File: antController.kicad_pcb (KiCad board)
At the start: 2 copper layers, 230 x 160 mm, 368 parts, among them J1 Lichtenprog_conn, J10 DB25_Male_MountingHoles, J11 DB25_Male_MountingHoles, J12 DB25_Male_MountingHoles, J13 DB25_Male_MountingHoles, J14 goldpins, J2 IDC10, J3 PWRINS, J4 DISP_OLED, J5 SMA CONN, J6 IDC10, J7 Lichtenprog_conn, J8 IDC10, J9 IDC10, K1 G5V-1, K10 G5V-1, K11 G5V-1, K12 G5V-1, K13 G5V-1, K14 G5V-1, K15 G5V-1, K2 G5V-1, K3 G5V-1, K4 G5V-1, K5 G5V-1, K6 G5V-1, K7 G5V-1, K8 G5V-1, K9 G5V-1, Q1 MMBT2222A, Q1 MMBT3904, Q10 BUZ11, Q11 BUZ11, Q12 BUZ11, Q13 BUZ11, Q14 BUZ11, Q15 BUZ11, Q16 BUZ11, Q17 BUZ11, Q18 BUZ11, Q19 2N7002, Q19 MMBT2222A, Q2 MMBT2222A, Q2 MMBT3904, Q20 2N7002, Q20 MMBT2222A, Q21 2N7002, Q21 MMBT2222A, Q22 2N7002, Q22 MMBT2222A, Q23 2N7002, Q23 MMBT2222A, Q24 2N7002, Q24 MMBT2222A, Q25 2N7002, Q25 MMBT2222A, Q26 2N7002, Q26 MMBT2222A, Q27 2N7002, Q27 MMBT2222A, Q28 2N7002, Q28 MMBT2222A, Q29 2N7002, Q29 MMBT2222A, Q3 BUZ11, Q30 2N7002, Q30 MMBT2222A, Q31 2N7002, Q31 MMBT2222A, Q32 2N7002, Q32 MMBT2222A, Q33 2N7002, Q33 MMBT2222A, Q4 BUZ11, Q5 BUZ11, Q6 BUZ11, Q7 BUZ11, Q8 BUZ11, Q9 BUZ11, SW1 B_RST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

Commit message: routing mostly done, fixing schematic issues
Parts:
- removed the Q1 at (84.0, 18.0)
- removed the Q19 at (185.7, 51.2)
- removed the Q19 at (300.0, 200.8)
- removed the Q2 at (77.0, 19.0)
- removed the Q20 at (185.7, 62.2)
- removed the Q20 at (313.5, 183.4)
- removed the Q21 at (300.0, 209.4)
- removed the Q21 at (185.7, 73.2)
- removed the Q22 at (204.5, 83.5)
- removed the Q22 at (287.1, 200.8)
- removed the Q23 at (287.1, 209.4)
- removed the Q23 at (185.7, 83.5)
- removed the Q24 at (204.5, 94.5)
- removed the Q24 at (312.8, 191.9)
- removed the Q25 at (185.7, 94.9)
- removed the Q25 at (300.6, 183.4)
- removed the Q26 at (195.7, 105.9)
- removed the Q26 at (300.0, 192.3)
- removed the Q27 at (287.1, 217.9)
- removed the Q27 at (195.7, 116.9)
- removed the Q28 at (195.7, 127.9)
- removed the Q28 at (300.0, 217.9)
- removed the Q29 at (326.4, 183.4)
- removed the Q29 at (195.7, 138.9)
- removed the Q30 at (325.7, 191.9)
- removed the Q30 at (195.7, 149.9)
- removed the Q31 at (287.1, 226.5)
- removed the Q31 at (204.8, 51.1)
- removed the Q32 at (204.8, 62.1)
- removed the Q32 at (312.8, 200.5)
- removed the Q33 at (204.6, 72.9)
- removed the Q33 at (287.1, 192.3)
- removed TP8, TP9: RLPAD, TestPoint:TestPoint_Pad_D1.0mm
- added C53: 100n, Capacitor_SMD:C_0402_1005Metric, F.Cu at (43.3, 149.0)
- added C54: 1n/DNP, Capacitor_SMD:C_0402_1005Metric, F.Cu at (58.4, 61.2)
- added C55: 1n/DNP, Capacitor_SMD:C_0402_1005Metric, F.Cu at (56.4, 61.2)
- added D44: 1N4148WS, Diode_SMD:D_SOD-323, F.Cu at (186.6, 53.8)
- added D45: 1N4148WS, Diode_SMD:D_SOD-323, F.Cu at (313.5, 100.6)
- added D46: 1N4148WS, Diode_SMD:D_SOD-323, F.Cu at (301.1, 100.6)
- added D47: 1N4148WS, Diode_SMD:D_SOD-323, F.Cu at (344.0, 82.1)
- added D48: 1N4148WS, Diode_SMD:D_SOD-323, F.Cu at (325.9, 98.7)
- added D49: 1N4148WS, Diode_SMD:D_SOD-323, F.Cu at (325.9, 106.9)
- added D50: 1N4148WS, Diode_SMD:D_SOD-323, F.Cu at (313.5, 108.8)
- added D51: 1N4148WS, Diode_SMD:D_SOD-323, F.Cu at (331.6, 90.4)
- added D52: 1N4148WS, Diode_SMD:D_SOD-323, F.Cu at (301.1, 108.8)
- added D53: 1N4148WS, Diode_SMD:D_SOD-323, F.Cu at (288.8, 100.6)
- added D54: 1N4148WS, Diode_SMD:D_SOD-323, F.Cu at (319.3, 90.4)
- added D55: 1N4148WS, Diode_SMD:D_SOD-323, F.Cu at (319.3, 82.1)
- added D56: 1N4148WS, Diode_SMD:D_SOD-323, F.Cu at (288.8, 108.8)
- added D57: 1N4148WS, Diode_SMD:D_SOD-323, F.Cu at (338.2, 98.7)
- added D58: 1N4148WS, Diode_SMD:D_SOD-323, F.Cu at (331.6, 82.1)
- added F1: FUSE_1206, Fuse:Fuse_1206_3216Metric, F.Cu at (161.0, 64.0)
- added F10: FUSE_1206, Fuse:Fuse_1206_3216Metric, F.Cu at (161.0, 86.5)
- added F11: FUSE_1206, Fuse:Fuse_1206_3216Metric, F.Cu at (161.0, 89.0)
- added F12: FUSE_1206, Fuse:Fuse_1206_3216Metric, F.Cu at (161.0, 91.5)
- added F13: FUSE_1206, Fuse:Fuse_1206_3216Metric, F.Cu at (161.0, 94.0)
- added F14: FUSE_1206, Fuse:Fuse_1206_3216Metric, F.Cu at (161.0, 96.5)
- added F15: FUSE_1206, Fuse:Fuse_1206_3216Metric, F.Cu at (161.0, 99.0)
- added F16: FUSE_1206, Fuse:Fuse_1206_3216Metric, F.Cu at (161.0, 101.5)
- added F2: FUSE_1206, Fuse:Fuse_1206_3216Metric, F.Cu at (161.0, 66.5)
- added F3: FUSE_1206, Fuse:Fuse_1206_3216Metric, F.Cu at (161.0, 69.0)
- added F4: FUSE_1206, Fuse:Fuse_1206_3216Metric, F.Cu at (161.0, 71.5)
- added F5: FUSE_1206, Fuse:Fuse_1206_3216Metric, F.Cu at (161.0, 74.0)
- added F6: FUSE_1206, Fuse:Fuse_1206_3216Metric, F.Cu at (161.0, 76.5)
- added F7: FUSE_1206, Fuse:Fuse_1206_3216Metric, F.Cu at (161.0, 79.0)
- added F8: FUSE_1206, Fuse:Fuse_1206_3216Metric, F.Cu at (161.0, 81.5)
- added F9: FUSE_1206, Fuse:Fuse_1206_3216Metric, F.Cu at (161.0, 84.0)
- added H11: SCRHOLE, MountingHole:MountingHole_3.2mm_M3_ISO7380_Pad, F.Cu at (36.5, 73.0)
- added H12: SCRHOLE, MountingHole:MountingHole_3.2mm_M3_ISO7380_Pad, F.Cu at (46.5, 73.0)
- added H13: SCRHOLE, MountingHole:MountingHole_3.2mm_M3_ISO7380_Pad, F.Cu at (36.5, 161.0)
- added H14: SCRHOLE, MountingHole:MountingHole_3.2mm_M3_ISO7380_Pad, F.Cu at (46.5, 161.0)
- added JP8: IOEX_A2_SEL, Jumper:SolderJumper-3_P2.0mm_Open_TrianglePad1.0x1.5mm, F.Cu at (204.2, 172.1)
- added Q19: MMBT3904, Package_TO_SOT_SMD:SOT-23, F.Cu at (185.7, 50.4)
- added Q20: MMBT3904, Package_TO_SOT_SMD:SOT-23, F.Cu at (308.9, 101.3)
- added Q21: MMBT3904, Package_TO_SOT_SMD:SOT-23, F.Cu at (296.6, 101.3)
- added Q22: MMBT3904, Package_TO_SOT_SMD:SOT-23, F.Cu at (339.4, 82.9)
- added Q23: MMBT3904, Package_TO_SOT_SMD:SOT-23, F.Cu at (321.3, 99.4)
- added Q24: MMBT3904, Package_TO_SOT_SMD:SOT-23, F.Cu at (321.3, 107.7)
- added Q25: MMBT3904, Package_TO_SOT_SMD:SOT-23, F.Cu at (308.9, 109.6)
- added Q26: MMBT3904, Package_TO_SOT_SMD:SOT-23, F.Cu at (327.1, 91.2)
- added Q27: MMBT3904, Package_TO_SOT_SMD:SOT-23, F.Cu at (296.6, 109.6)
- added Q28: MMBT3904, Package_TO_SOT_SMD:SOT-23, F.Cu at (284.2, 101.3)
- added Q29: MMBT3904, Package_TO_SOT_SMD:SOT-23, F.Cu at (314.7, 91.2)
- added Q30: MMBT3904, Package_TO_SOT_SMD:SOT-23, F.Cu at (314.7, 82.9)
- added Q31: MMBT3904, Package_TO_SOT_SMD:SOT-23, F.Cu at (284.2, 109.6)
- added Q32: MMBT3904, Package_TO_SOT_SMD:SOT-23, F.Cu at (333.7, 99.4)
- added Q33: MMBT3904, Package_TO_SOT_SMD:SOT-23, F.Cu at (327.1, 82.9)
- added SW5: B3, Button_Switch_SMD:SW_SPST_TL3342, F.Cu at (38.3, 150.6)
- D1, D2, D3, D4: footprint LED_THT:LED_D3.0mm -> LED_SMD:LED_0603_1608Metric
- D10, D11, D12, D13, D14, D15, D16, D17, D18, D19, D20, D21, D22, D23, D24, D25, D26, D27, D28, D29, D30, D31, D32, D33, D34, D35, D36, D37, D38, D39, D40, D41, D42, D43, D5, D6, D7, D8, D9: value LED -> LED_RED; footprint Diode_SMD:D_0603_1608Metric -> LED_SMD:LED_0603_1608Metric
- H10, H7, H8, H9: value SCRHOLE -> HOLE_B2
- J14: value goldpins -> Proto_matrix_14x10; footprint Connector_PinHeader_2.54mm:PinHeader_1x10_P2.54mm_Vertical -> Critbit_lib:Proto_matrix_14x10
- J4: value DISP_OLED -> FRONT_PANEL; footprint Connector_PinHeader_2.54mm:PinHeader_1x04_P2.54mm_Vertical -> Connector_PinHeader_2.54mm:PinHeader_2x08_P2.54mm_Horizontal
- R107, R108, R109, R110, R111, R112, R113, R114, R115, R116, R117, R118, R119, R120, R121, R122, R123, R124, R125, R126, R127, R128, R129, R130, R131, R132, R133, R134, R135, R136, R137, R138, R139, R140, R141, R142, R143, R144, R145: value 10k -> 33k
- R21, R22, R23, R24, R25, R26, R27, R29, R30, R31, R32, R33: value 10k -> 10k_1206
- SW1, SW2, SW3, SW4: footprint Button_Switch_THT:SW_Tactile_SPST_Angled_PTS645Vx83-2LFS -> Button_Switch_SMD:SW_SPST_TL3342
- moved D12 308.8 mm to (69.0, 86.0), turned to 90 degrees
- moved R114 307.8 mm to (69.0, 89.5), turned to 90 degrees
- moved D7 303.0 mm to (94.8, 44.0), turned to 90 degrees
- moved R109 301.8 mm to (94.8, 47.5), turned to 90 degrees
- moved Q1 294.9 mm to (36.1, 36.9), turned to -90 degrees
- moved D16 290.4 mm to (69.0, 114.0), turned to 90 degrees
- moved D8 290.2 mm to (69.0, 58.0), turned to 90 degrees
- moved R118 289.5 mm to (69.0, 117.5), turned to 90 degrees
- moved R110 289.1 mm to (69.0, 61.5), turned to 90 degrees
- moved D10 288.3 mm to (69.0, 72.0), turned to 90 degrees
- moved R112 287.2 mm to (69.0, 75.5), turned to 90 degrees
- moved Q2 286.8 mm to (40.5, 37.0), turned to -90 degrees
- moved D14 285.8 mm to (69.0, 100.0), turned to 90 degrees
- moved R116 284.8 mm to (69.0, 103.5), turned to 90 degrees
- moved D20 284.0 mm to (68.9, 142.5), turned to 90 degrees
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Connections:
- net Net-(J3-Pad4) renamed /5V_IN
- C3 pad 1: /ESP_EN -> /B2
- C8 pad 1: /ESP_BOOT -> /B2
- D2 pad 2: Net-(C10-Pad1) -> +3.3V
- D3 pad 2: +3.3V -> /B2
- J11 pad 10: /Back connectors/SINK2 -> Net-(J11-Pad10)
- J11 pad 14: /Back connectors/SINK16 -> Net-(J11-Pad14)
- J11 pad 15: /Back connectors/SINK14 -> Net-(J11-Pad15)
- J11 pad 17: /Back connectors/SINK11 -> Net-(J11-Pad17)
- J11 pad 18: /Back connectors/SINK9 -> Net-(J11-Pad18)
- J11 pad 19: /Back connectors/SINK8 -> Net-(J11-Pad19)
- J11 pad 2: /Back connectors/SINK15 -> Net-(J11-Pad2)
- J11 pad 20: /Back connectors/SINK6 -> Net-(J11-Pad20)
- J11 pad 22: /Back connectors/SINK3 -> Net-(J11-Pad22)
- J11 pad 23: /Back connectors/SINK1 -> Net-(J11-Pad23)
- J11 pad 3: /Back connectors/SINK13 -> Net-(J11-Pad3)
- J11 pad 4: /Back connectors/SINK12 -> Net-(J11-Pad4)
- J11 pad 5: /Back connectors/SINK10 -> Net-(J11-Pad5)
- J11 pad 7: /Back connectors/SINK7 -> Net-(J11-Pad7)
- J11 pad 8: /Back connectors/SINK5 -> Net-(J11-Pad8)
- J11 pad 9: /Back connectors/SINK4 -> Net-(J11-Pad9)
- J13 pad 10: Net-(C26-Pad1) -> Net-(J13-Pad10)
- J13 pad 11: Net-(C25-Pad1) -> Net-(J13-Pad11)
- J13 pad 12: Net-(C23-Pad1) -> Net-(J13-Pad12)
- J13 pad 19: Net-(C32-Pad1) -> Net-(J13-Pad19)
- J13 pad 20: Net-(C30-Pad1) -> Net-(J13-Pad20)
- J13 pad 21: Net-(C29-Pad1) -> Net-(J13-Pad21)
- J13 pad 22: Net-(C27-Pad1) -> Net-(J13-Pad22)
- J13 pad 24: Net-(C24-Pad1) -> Net-(J13-Pad24)
- J13 pad 25: Net-(C22-Pad1) -> Net-(J13-Pad25)
- J13 pad 6: Net-(C33-Pad1) -> Net-(J13-Pad6)
- J13 pad 7: Net-(C31-Pad1) -> Net-(J13-Pad7)
- J13 pad 9: Net-(C28-Pad1) -> Net-(J13-Pad9)
- J4 pad 1: /SDA -> unconnected-(J4-Pad1)
- J4 pad 2: /SCL -> +5V
- J4 pad 3: +3.3V -> unconnected-(J4-Pad3)
- J4 pad 4: GND -> /B2
- J6 pad 7: Net-(J6-Pad7) -> Net-(J6-Pad10)
- J6 pad 8: Net-(J6-Pad7) -> Net-(J6-Pad10)
- J7 pad 6: Net-(J6-Pad7) -> Net-(J6-Pad10)
- J8 pad 3: /Back connectors/SCL_5V -> /SCL_5V
- J8 pad 5: /Back connectors/SDA_5V -> /SDA_5V
- K1 pad 2: /Back connectors/Relay1/VCOIL -> +5VD
- K10 pad 2: /Back connectors/Relay10/VCOIL -> +5VD
- K11 pad 2: /Back connectors/Relay11/VCOIL -> +5VD
- K12 pad 2: /Back connectors/Relay12/VCOIL -> +5VD
- K13 pad 2: /Back connectors/Relay13/VCOIL -> +5VD
- K14 pad 2: /Back connectors/Relay14/VCOIL -> +5VD
- K15 pad 2: /Back connectors/Relay15/VCOIL -> +5VD
- K2 pad 2: /Back connectors/Relay2/VCOIL -> +5VD
- K3 pad 2: /Back connectors/Relay3/VCOIL -> +5VD
- K4 pad 2: /Back connectors/Relay4/VCOIL -> +5VD
- K5 pad 2: /Back connectors/Relay5/VCOIL -> +5VD
- K6 pad 2: /Back connectors/Relay6/VCOIL -> +5VD
- K7 pad 2: /Back connectors/Relay7/VCOIL -> +5VD
- K8 pad 2: /Back connectors/Relay8/VCOIL -> +5VD
- K9 pad 2: /Back connectors/Relay9/VCOIL -> +5VD
- Q1 pad 3: /ESP_EN -> /B2
- Q2 pad 3: /ESP_BOOT -> /B2
- R15 pad 1: /LED_STATUS -> GND
- R21 pad 1: Net-(C22-Pad1) -> Net-(J13-Pad25)
- R21 pad 2: Net-(R21-Pad2) -> Net-(C22-Pad1)
- R22 pad 1: Net-(C23-Pad1) -> Net-(J13-Pad12)
- R22 pad 2: Net-(R22-Pad2) -> Net-(C23-Pad1)
- R23 pad 1: Net-(C24-Pad1) -> Net-(J13-Pad24)
- R23 pad 2: Net-(R23-Pad2) -> Net-(C24-Pad1)
- R24 pad 1: Net-(C25-Pad1) -> Net-(J13-Pad11)
- R24 pad 2: Net-(R24-Pad2) -> Net-(C25-Pad1)
- R25 pad 1: Net-(C26-Pad1) -> Net-(J13-Pad10)
- R25 pad 2: Net-(R25-Pad2) -> Net-(C26-Pad1)
- R26 pad 1: Net-(C27-Pad1) -> Net-(J13-Pad22)
- R26 pad 2: Net-(R26-Pad2) -> Net-(C27-Pad1)
- R27 pad 1: Net-(C28-Pad1) -> Net-(J13-Pad9)
- R27 pad 2: Net-(R27-Pad2) -> Net-(C28-Pad1)
- R29 pad 1: Net-(C29-Pad1) -> Net-(J13-Pad21)
- R29 pad 2: Net-(R29-Pad2) -> Net-(C29-Pad1)
- R3 pad 1: Net-(R3-Pad1) -> /B2
- R30 pad 1: Net-(C30-Pad1) -> Net-(J13-Pad20)
- R30 pad 2: Net-(R30-Pad2) -> Net-(C30-Pad1)
- R31 pad 1: Net-(C31-Pad1) -> Net-(J13-Pad7)
- R31 pad 2: Net-(R31-Pad2) -> Net-(C31-Pad1)
- R32 pad 1: Net-(C32-Pad1) -> Net-(J13-Pad19)
- R32 pad 2: Net-(R32-Pad2) -> Net-(C32-Pad1)
- R33 pad 1: Net-(C33-Pad1) -> Net-(J13-Pad6)
- R33 pad 2: Net-(R33-Pad2) -> Net-(C33-Pad1)
- R35 pad 2: /OUT_BUF_ENA -> /Back connectors/B2_OUT_BUF_ENA
- R4 pad 1: /ESP_BOOT -> /B2
- R5 pad 1: /ESP_EN -> /B2
- SW1 pad 2: /ESP_EN -> /B2
- SW2 pad 2: /ESP_BOOT -> /B2
- U10 pad 11: Net-(R36-Pad2) -> Net-(C33-Pad1)
- U10 pad 12: /IO27 -> unconnected-(U10-Pad12)
- U10 pad 13: Net-(R36-Pad2) -> Net-(C32-Pad1)
- U10 pad 14: /IO26 -> unconnected-(U10-Pad14)
- U10 pad 15: Net-(R36-Pad2) -> Net-(C31-Pad1)
- U10 pad 16: /IO25 -> unconnected-(U10-Pad16)
- U10 pad 17: Net-(R36-Pad2) -> Net-(C30-Pad1)
- U10 pad 18: /IO23 -> unconnected-(U10-Pad18)
- U10 pad 2: Net-(R30-Pad2) -> Net-(R36-Pad2)
- U10 pad 3: unconnected-(U10-Pad3) -> /IO23
- U10 pad 4: Net-(R31-Pad2) -> Net-(R36-Pad2)
- U10 pad 5: unconnected-(U10-Pad5) -> /IO25
- U10 pad 6: Net-(R32-Pad2) -> Net-(R36-Pad2)
- U10 pad 7: unconnected-(U10-Pad7) -> /IO26
- U10 pad 8: Net-(R33-Pad2) -> Net-(R36-Pad2)
- U10 pad 9: unconnected-(U10-Pad9) -> /IO27
- U14 pad 3: /Back connectors/OC5_C -> /Back connectors/OC5_E
- U14 pad 4: /Back connectors/OC5_E -> /Back connectors/OC5_C
- U15 pad 3: /Back connectors/OC6_C -> /Back connectors/OC6_E
- U15 pad 4: /Back connectors/OC6_E -> /Back connectors/OC6_C
- U16 pad 3: /Back connectors/OC7_C -> /Back connectors/OC7_E
- U16 pad 4: /Back connectors/OC7_E -> /Back connectors/OC7_C
- U17 pad 3: /Back connectors/OC8_C -> /Back connectors/OC8_E
- U17 pad 4: /Back connectors/OC8_E -> /Back connectors/OC8_C
- U2 pad 24: Net-(R3-Pad1) -> /B2
- U2 pad 25: /ESP_BOOT -> /B2
- U2 pad 3: /ESP_EN -> /B2
- U2 pad 9: /LED_STATUS -> /B2
- U3 pad 2: unconnected-(U3-Pad2) -> Net-(C10-Pad1)
- U3 pad 3: unconnected-(U3-Pad3) -> +5V
- U5 pad 22: /Back connectors/SCL_5V -> /SCL_5V
- U5 pad 23: /Back connectors/SDA_5V -> /SDA_5V
- U6 pad 3: unconnected-(U6-Pad3) -> Net-(JP8-Pad2)
- U7 pad 11: Net-(R29-Pad2) -> Net-(C29-Pad1)
- U7 pad 13: Net-(R27-Pad2) -> Net-(C28-Pad1)
- U7 pad 15: Net-(R26-Pad2) -> Net-(C27-Pad1)
- U7 pad 17: Net-(R25-Pad2) -> Net-(C26-Pad1)
- U7 pad 2: Net-(R21-Pad2) -> Net-(C22-Pad1)
- U7 pad 4: Net-(R22-Pad2) -> Net-(C23-Pad1)
- U7 pad 6: Net-(R23-Pad2) -> Net-(C24-Pad1)
- U7 pad 8: Net-(R24-Pad2) -> Net-(C25-Pad1)
- U8 pad 1: /OUT_BUF_ENA -> /Back connectors/B2_OUT_BUF_ENA
- U8 pad 19: /OUT_BUF_ENA -> /Back connectors/B2_OUT_BUF_ENA
- U9 pad 3: unconnected-(U9-Pad3) -> Net-(JP8-Pad2)
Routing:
- net /B2: track 0.00 -> 305.5 mm, vias 0 -> 1
- net /IO18: track 0.00 -> 238.0 mm, vias 0 -> 4
- net /IO23: track 0.00 -> 227.6 mm, vias 0 -> 2
- net /IO22: track 0.00 -> 226.3 mm, vias 0 -> 2
- net /IO17: track 0.00 -> 225.9 mm, vias 0 -> 2
- net /IO21: track 0.00 -> 223.3 mm, vias 0 -> 2
- net /IO16: track 0.00 -> 223.2 mm, vias 0 -> 2
- net /IO19: track 0.00 -> 221.7 mm, vias 0 -> 2
- net /IN_BUFF_ENA: track 0.00 -> 218.0 mm, vias 0 -> 2
- net /IO15: track 0.00 -> 217.0 mm, vias 0 -> 2
- net /IO14: track 0.00 -> 209.9 mm
- net /IO25: track 0.00 -> 206.6 mm, vias 0 -> 2
- net /IO26: track 0.00 -> 201.8 mm, vias 0 -> 2
- net /IO27: track 0.00 -> 201.0 mm
- net GND: track 52.5 -> 180.2 mm, vias 0 -> 14
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- added copper zone on F.Cu, net +VDC
- added copper zone on F.Cu, net /5V_IN
- added copper zone on B.Cu, net GND
- added copper zone on B.Cu, net GND2
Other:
- outline, holes or cut-outs redrawn

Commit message: succesfully run replicate layout on relays
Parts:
- moved D55 141.4 mm to (196.6, 152.5), turned to 90 degrees
- moved D48 139.8 mm to (186.6, 86.1), turned to 90 degrees
- moved D47 138.7 mm to (205.4, 86.0), turned to 90 degrees
- moved D57 136.9 mm to (205.7, 64.7), turned to 90 degrees
- moved Q23 136.6 mm to (185.7, 82.7)
- moved D51 136.2 mm to (196.6, 108.5), turned to 90 degrees
- moved Q30 136.2 mm to (195.7, 149.1)
- moved Q22 134.9 mm to (204.5, 82.6)
- moved Q32 134.4 mm to (204.8, 61.3)
- moved D54 132.9 mm to (196.6, 141.5), turned to 90 degrees
- moved Q26 132.1 mm to (195.7, 105.1)
- moved D45 131.9 mm to (186.6, 64.8), turned to 90 degrees
- moved Q20 129.6 mm to (185.7, 61.4)
- moved Q29 127.9 mm to (195.7, 138.1)
- moved D50 127.4 mm to (186.6, 97.5), turned to 90 degrees
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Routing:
- net +5VD: track 6.71 -> 114.8 mm
- net /Back connectors/RL_CTRL1: track 5.41 -> 94.4 mm, vias 0 -> 2
- net /Back connectors/RL_CTRL2: track 0.00 -> 54.1 mm, vias 0 -> 2
- net /Back connectors/RL_CTRL3: track 0.00 -> 42.4 mm, vias 0 -> 2
- net /Back connectors/RL_CTRL5: track 0.00 -> 31.6 mm, vias 0 -> 2
- net /Back connectors/RL_CTRL7: track 0.00 -> 20.8 mm, vias 0 -> 2
- net GND2: track 75.3 -> 55.1 mm
- net /Back connectors/RL7_A: track 55.7 -> 43.8 mm
- net /Back connectors/RL_CTRL14: track 0.00 -> 5.41 mm
- net /Back connectors/RL_CTRL13: track 0.00 -> 5.41 mm
- net /Back connectors/RL_CTRL15: track 0.00 -> 5.41 mm
- net /Back connectors/RL_CTRL6: track 0.00 -> 5.41 mm
- net /Back connectors/RL_CTRL4: track 0.00 -> 5.41 mm
- net /Back connectors/RL_CTRL12: track 0.00 -> 5.41 mm
- net /Back connectors/RL_CTRL11: track 0.00 -> 5.41 mm
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
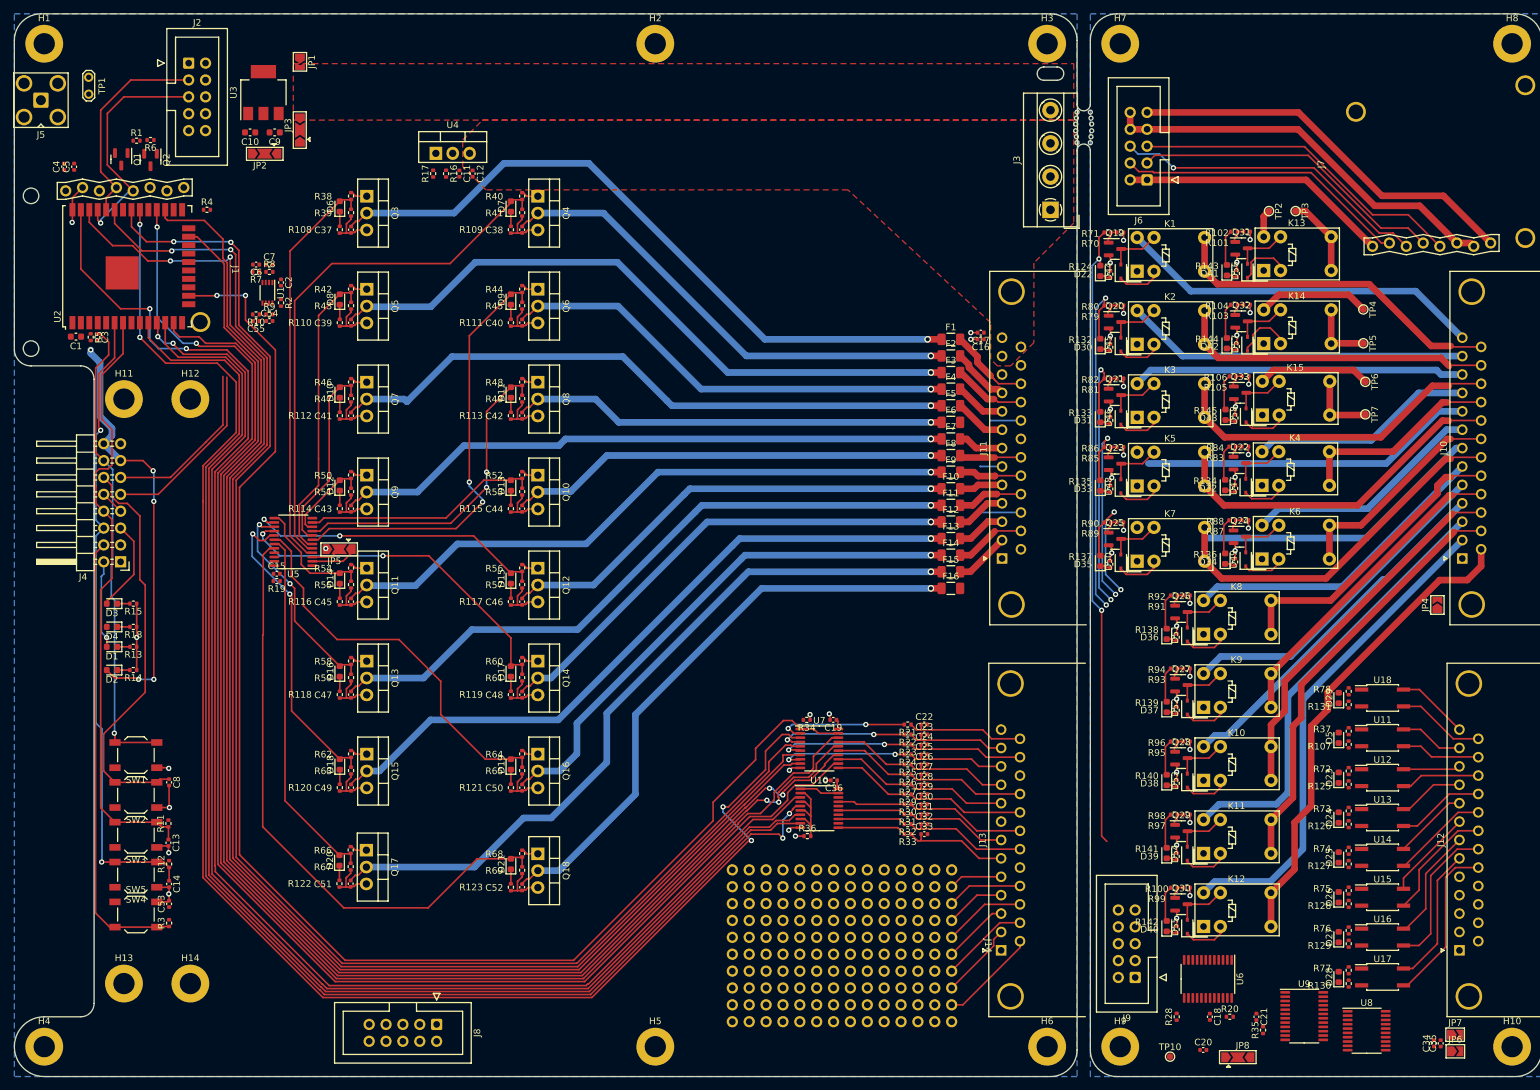
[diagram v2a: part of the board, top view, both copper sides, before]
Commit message: finish routing and silk
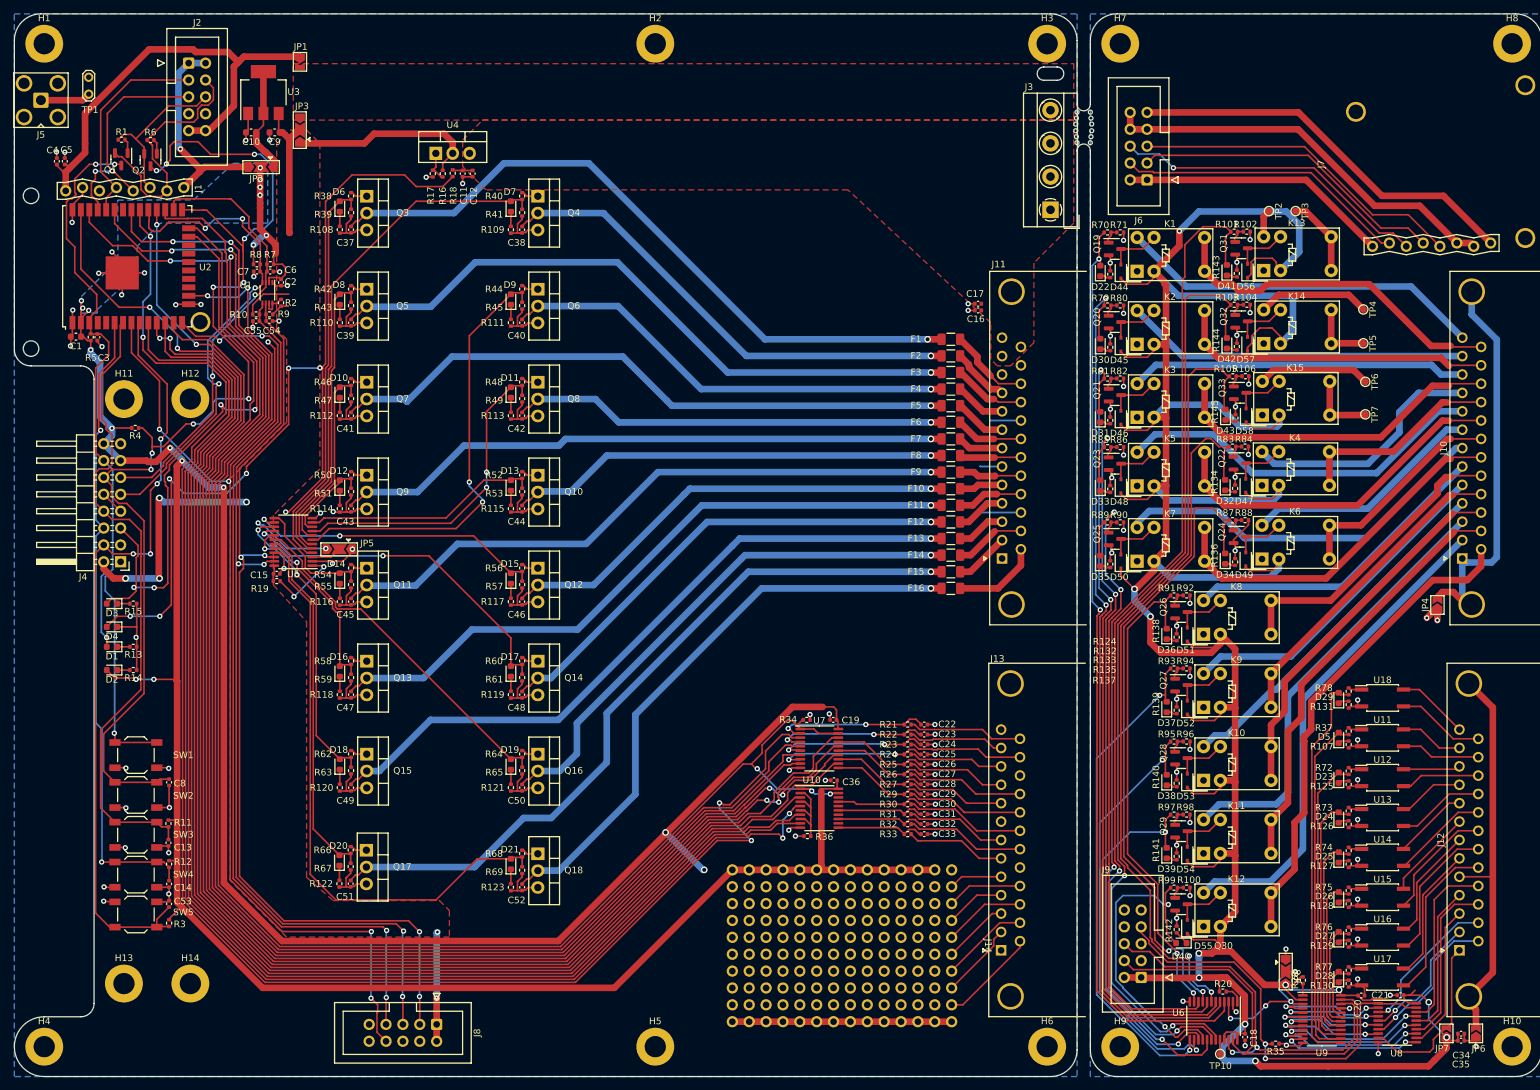
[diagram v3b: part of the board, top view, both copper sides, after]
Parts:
- moved R18 83.5 mm to (86.0, 39.0), turned to 90 degrees
- moved R4 34.6 mm to (38.2, 77.3), turned to 180 degrees
- moved C20 25.2 mm to (222.8, 162.8)
- moved C21 21.9 mm to (228.7, 162.8), turned to 180 degrees
- moved R28 19.8 mm to (214.0, 160.5)
- moved JP8 14.8 mm to (211.4, 159.2), turned to -90 degrees
- moved TP10 7.56 mm to (201.6, 171.6)
- moved U6 6.36 mm to (200.6, 166.6)
- moved C18 6.11 mm to (205.3, 169.1)
- moved U8 4.75 mm to (228.2, 166.9)
- moved C16 4.37 mm to (165.1, 59.6)
- moved C17 4.37 mm to (165.1, 58.6)
- moved C34 4.32 mm to (237.8, 168.6), turned to 180 degrees
- moved JP6 4.11 mm to (240.1, 168.5), turned to 90 degrees
- moved R20 3.94 mm to (201.9, 162.2), turned to 180 degrees
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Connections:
- C21 pad 2: GND -> GND2
- C3 pad 1: /B2 -> /ESP_EN
- C34 pad 2: +5V -> +5VD
- C35 pad 2: +5V -> +5VD
- C53 pad 1: /B2 -> /B4
- C8 pad 1: /B2 -> /ESP_BOOT
- D3 pad 2: /B2 -> /LED_STATUS
- D4 pad 1: Net-(D4-Pad1) -> GND
- D4 pad 2: +VDC -> Net-(R18-Pad1)
- J14 pad A10: unconnected-(J14-PadA10) -> +3.3V
- J14 pad A11: unconnected-(J14-PadA11) -> +3.3V
- J14 pad A12: unconnected-(J14-PadA12) -> +3.3V
- J14 pad A13: unconnected-(J14-PadA13) -> +3.3V
- J14 pad A14: unconnected-(J14-PadA14) -> +3.3V
- J14 pad A2: unconnected-(J14-PadA2) -> +3.3V
- J14 pad A3: unconnected-(J14-PadA3) -> +3.3V
- J14 pad A4: unconnected-(J14-PadA4) -> +3.3V
- J14 pad A5: unconnected-(J14-PadA5) -> +3.3V
- J14 pad A6: unconnected-(J14-PadA6) -> +3.3V
- J14 pad A7: unconnected-(J14-PadA7) -> +3.3V
- J14 pad A8: unconnected-(J14-PadA8) -> +3.3V
- J14 pad A9: unconnected-(J14-PadA9) -> +3.3V
- J14 pad J10: unconnected-(J14-PadJ10) -> GND
- J14 pad J11: unconnected-(J14-PadJ11) -> GND
- J14 pad J12: unconnected-(J14-PadJ12) -> GND
- J14 pad J13: unconnected-(J14-PadJ13) -> GND
- J14 pad J14: unconnected-(J14-PadJ14) -> GND
- J14 pad J2: unconnected-(J14-PadJ2) -> GND
- J14 pad J3: unconnected-(J14-PadJ3) -> GND
- J14 pad J4: unconnected-(J14-PadJ4) -> GND
- J14 pad J5: unconnected-(J14-PadJ5) -> GND
- J14 pad J6: unconnected-(J14-PadJ6) -> GND
- J14 pad J7: unconnected-(J14-PadJ7) -> GND
- J14 pad J8: unconnected-(J14-PadJ8) -> GND
- J14 pad J9: unconnected-(J14-PadJ9) -> GND
- J4 pad 12: /B2 -> /ESP_BOOT
- J4 pad 14: /B2 -> /ESP_EN
- J4 pad 4: /B2 -> /B4
- J4 pad 5: /B2 -> /LED_STATUS
- JP7 pad 1: +5V -> +5VD
- Q1 pad 3: /B2 -> /ESP_EN
- Q2 pad 3: /B2 -> /ESP_BOOT
- R18 pad 1: GND -> Net-(R18-Pad1)
- R18 pad 2: Net-(D4-Pad1) -> +VDC
- R3 pad 1: /B2 -> /B4
- R4 pad 1: /B2 -> /ESP_BOOT
- R5 pad 1: /B2 -> /ESP_EN
- SW1 pad 2: /B2 -> /ESP_EN
- SW2 pad 2: /B2 -> /ESP_BOOT
- SW5 pad 2: /B2 -> /B4
- U2 pad 24: /B2 -> /LED_STATUS
- U2 pad 25: /B2 -> /ESP_BOOT
- U2 pad 3: /B2 -> /ESP_EN
- U2 pad 9: /B2 -> /B4
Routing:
- net +3.3V: track 67.3 -> 491.1 mm, vias 5 -> 18
- net +5VD: track 114.8 -> 514.2 mm, vias 0 -> 11
- net /B2: track 305.5 -> 97.0 mm, vias 1 -> 0
- net /ESP_BOOT: track 0.00 -> 173.8 mm, vias 0 -> 10
- net /OUT_BUF_ENA: track 0.00 -> 157.8 mm, vias 0 -> 5
- net /Back connectors/RL_CTRL13: track 5.41 -> 152.3 mm, vias 0 -> 2
- net /SCL_5V: track 0.00 -> 140.5 mm, vias 0 -> 4
- net /I2C_RST: track 0.00 -> 140.1 mm, vias 0 -> 4
- net Net-(R18-Pad1): track 0.00 -> 139.2 mm, vias 0 -> 7
- net /SDA_5V: track 0.00 -> 139.1 mm, vias 0 -> 4
- net /Back connectors/RL_CTRL14: track 5.41 -> 142.2 mm, vias 0 -> 2
- net /Back connectors/RL_CTRL15: track 5.41 -> 130.0 mm, vias 0 -> 2
- net /B4: track 0.00 -> 117.0 mm, vias 0 -> 4
- net /ESP_EN: track 0.00 -> 107.4 mm, vias 0 -> 3
- net GND: track 180.2 -> 286.7 mm, vias 14 -> 56
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- added copper zone on B.Cu, net +3.3V
- added copper zone on F.Cu, net +5V

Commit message: prod files
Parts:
- added C56: 220u, Capacitor_THT:CP_Radial_D8.0mm_P3.50mm, F.Cu at (205.8, 158.9)
- added C57: 220u, Capacitor_THT:CP_Radial_D8.0mm_P3.50mm, F.Cu at (66.8, 32.7)
- added J15: VIN, Critbit_lib:DG235-5.0, F.Cu at (173.5, 34.5)
- added J16: VIN, Critbit_lib:DG235-5.0, F.Cu at (173.5, 39.5)
- added J17: VIN, Critbit_lib:DG235-5.0, F.Cu at (173.5, 44.5)
- added kibuzzard-6394C445: G***, kibuzzard-6394C445, F.Cu at (95.0, 167.6)
- added kibuzzard-6394C445: G***, kibuzzard-6394C445, F.Cu at (232.8, 19.6)
- added kibuzzard-6394C46A: G***, kibuzzard-6394C46A, F.Cu at (95.0, 169.6)
- added kibuzzard-6394C46A: G***, kibuzzard-6394C46A, F.Cu at (232.8, 21.6)
- added kibuzzard-6394C47E: G***, kibuzzard-6394C47E, F.Cu at (232.7, 23.6)
- added kibuzzard-6394C47E: G***, kibuzzard-6394C47E, F.Cu at (95.0, 171.5)
- added kibuzzard-6394C560: G***, kibuzzard-6394C560, F.Cu at (95.9, 165.7)
- added kibuzzard-6394C560: G***, kibuzzard-6394C560, F.Cu at (233.7, 17.7)
- J3: value PWRINS -> VIN; footprint TerminalBlock_MetzConnect:TerminalBlock_MetzConnect_Type055_RT01504HDWU_1x04_P5.00mm_Horizontal -> Critbit_lib:DG235-5.0
- R21, R22, R23, R24, R25, R26, R27, R29, R30, R31, R32, R33: footprint Resistor_SMD:R_0402_1005Metric -> Resistor_SMD:R_1206_3216Metric_Pad1.30x1.75mm_HandSolder
- moved J3 15.2 mm to (173.5, 29.5)
- moved R21 11.9 mm to (161.0, 112.0)
- moved R22 11.1 mm to (161.0, 114.5)
- moved C22 11.0 mm to (152.5, 112.0), turned to 180 degrees
- moved R23 10.3 mm to (161.0, 117.0)
- moved C23 10.1 mm to (152.5, 114.5), turned to 180 degrees
- moved R24 9.55 mm to (161.0, 119.5)
- moved C24 9.17 mm to (152.5, 117.0), turned to 180 degrees
- moved R25 8.85 mm to (161.0, 122.0)
- moved C25 8.31 mm to (152.5, 119.5), turned to 180 degrees
- moved R26 8.20 mm to (161.0, 124.5)
- moved R27 7.63 mm to (161.0, 127.0)
- moved C26 7.50 mm to (152.5, 122.0), turned to 180 degrees
- moved R29 7.16 mm to (161.0, 129.5)
- moved R30 6.80 mm to (161.0, 132.0)
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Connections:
- J3 pad 1: GND -> /5V_IN
- J6 pad 7: Net-(J6-Pad10) -> Net-(J6-Pad8)
- J6 pad 8: Net-(J6-Pad10) -> Net-(J6-Pad8)
- J6 pad 9: Net-(J6-Pad9) -> Net-(J6-Pad10)
- J7 pad 6: Net-(J6-Pad10) -> Net-(J6-Pad8)
- J7 pad 7: Net-(J6-Pad10) -> Net-(J6-Pad8)
- J7 pad 8: Net-(J6-Pad9) -> Net-(J6-Pad10)
- J9 pad 3: unconnected-(J9-Pad3) -> /Back connectors/B2_SCL
- J9 pad 4: /Back connectors/B2_SCL -> unconnected-(J9-Pad4)
- J9 pad 5: unconnected-(J9-Pad5) -> /Back connectors/B2_SDA
- J9 pad 6: /Back connectors/B2_SDA -> unconnected-(J9-Pad6)
- J9 pad 7: /Back connectors/B2_OUT_BUF_ENA -> unconnected-(J9-Pad7)
- J9 pad 8: unconnected-(J9-Pad8) -> /Back connectors/B2_OUT_BUF_ENA
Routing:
- net Net-(J6-Pad9): track 59.9 -> 0.00 mm
- net Net-(J6-Pad8): track 0.00 -> 59.0 mm
- net Net-(J13-Pad6): track 15.1 -> 7.12 mm
- net Net-(C22-Pad1): track 23.1 -> 31.0 mm
- net Net-(J13-Pad19): track 18.0 -> 10.4 mm
- net Net-(J13-Pad7): track 15.2 -> 8.04 mm
- net Net-(C23-Pad1): track 23.2 -> 29.8 mm
- net Net-(J13-Pad20): track 18.1 -> 11.4 mm
- net Net-(J13-Pad21): track 17.5 -> 11.2 mm
- net Net-(C24-Pad1): track 22.8 -> 28.8 mm
- net Net-(J13-Pad9): track 14.7 -> 9.47 mm
- net Net-(C25-Pad1): track 22.7 -> 27.9 mm
- net Net-(J13-Pad22): track 17.6 -> 13.4 mm
- net Net-(C33-Pad1): track 13.4 -> 17.0 mm
- net +5V: track 111.1 -> 114.4 mm
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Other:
- outline, holes or cut-outs redrawn
- board text added: "antController rev. 1.0 (C) Cr1tbit + SP5GNI 12.2022"
- board text added: "antController upper board rev. 1.0 (C) Cr1tbit + SP5GNI 12.2022"
